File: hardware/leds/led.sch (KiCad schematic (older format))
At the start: 76 parts, among them P1 ICD3 header, P2 ICD3 header, U1 PIC18F2450, U2 74HC594, U3 74HC594, U4 74HC594, U5 74HC594, X1 20 MHz

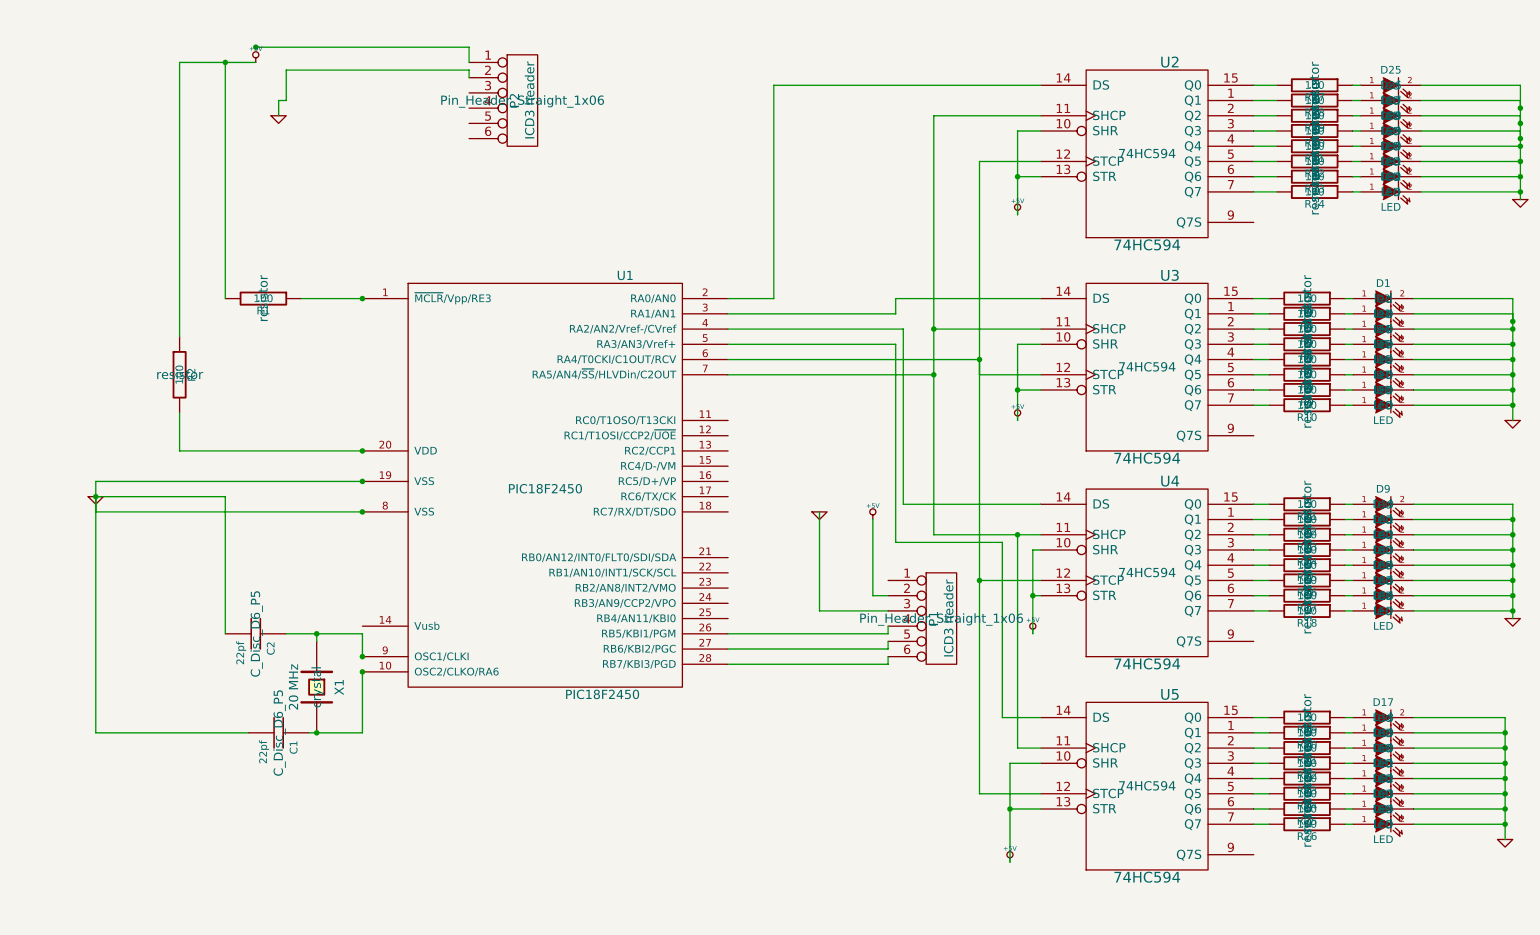
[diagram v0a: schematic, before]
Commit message: leds on the edge. routing not quite done yet
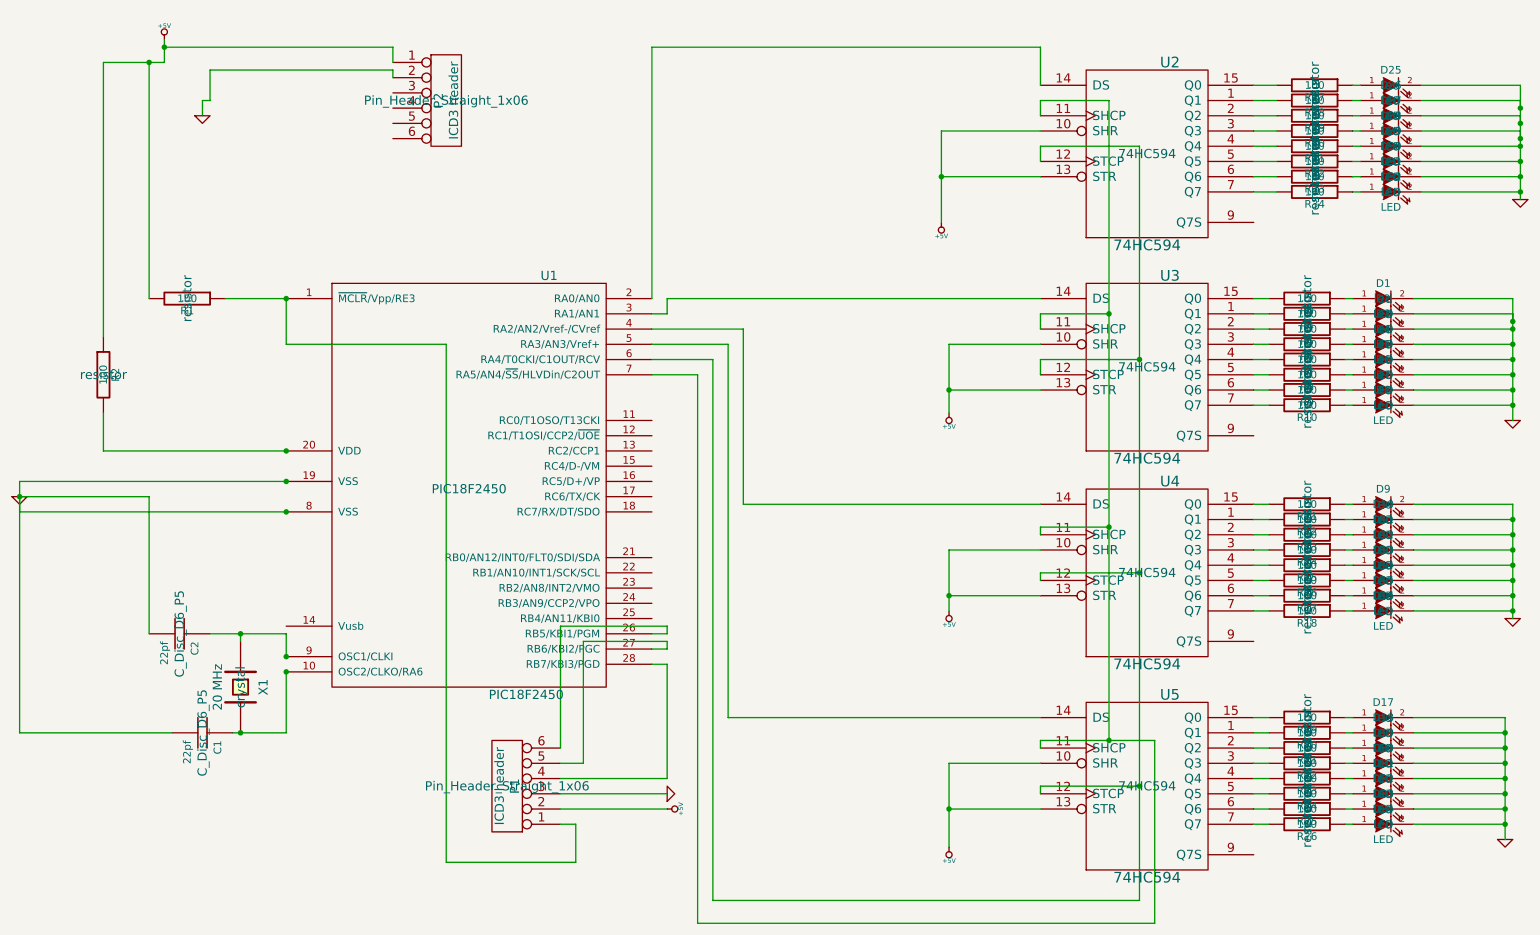
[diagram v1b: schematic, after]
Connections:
- net +5V: now also P2.1
- net at R1.1, U1.1 (~MCLR~/Vpp/RE3): now also P1.1
- net at U1.26 (RB5/KBI1/PGM): now also P1.6; no longer P1.4
- net at U1.28 (RB7/KBI3/PGD): now also P1.4; no longer P1.6
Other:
- moved on the sheet: C1, C2, P1, P2, R1, R2, U1, X1

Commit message: More compact design
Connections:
- net VCC is gone; now on net +5V: U2.16 (VCC), U3.16 (VCC), U4.16 (VCC), U5.16 (VCC)
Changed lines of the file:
@@
 Connection ~ 1400 850
 Wire Wire Line
-	3000 750  1500 750
+	1300 750  3000 750
 Connection ~ 1500 750
+$Comp
+L VCC #PWR?
+U 1 1 56CABC2B
+P 1300 650
+F 0 "#PWR?" H 1300 750 30  0001 C CNN
+F 1 "VCC" H 1300 750 30  0000 C CNN
+F 2 "" H 1300 650 60  0000 C CNN
+F 3 "" H 1300 650 60  0000 C CNN
+	1    1300 650
+	1    0    0    -1
+$EndComp
+Wire Wire Line
+	1300 650  1300 750
 $EndSCHEMATC
